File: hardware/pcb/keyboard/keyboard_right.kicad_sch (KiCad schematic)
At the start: 29 parts, among them J1 SM04B-SRSS-TB, J2 PJ320D, J3 HRO_TYPE-C-31-M-12, J4 FFC Connector, SW29 PTS845, U3 DT1446-04S, U4 XC6220B331MR-G, U5 STM32G431KBTx, Y1 8MHz

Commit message: usb hib init
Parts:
- added R9: 1k, PCM_Resistor_SMD_AKL:R_0603_1608Metric, symbol Device:R
- added R9: 10k, PCM_Resistor_SMD_AKL:R_0603_1608Metric, symbol Device:R
- added R9: 5.1k, PCM_Resistor_SMD_AKL:R_0603_1608Metric, symbol Device:R
- J4: value FFC Connector -> HRS_FH34SRJ-12S-0.5SH(50)
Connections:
- net +3V3: now also R9.2
- net ACCS_1: now also U5.9 (PA4), R9.1; no longer U5.5 (PA0)
- net ACCS_3: now also R9.1, R9.2
- net CSEL0: now also U5.5 (PA0); no longer U5.9 (PA4)
- net GND: now also R9.1
- net VBUS: now also R9.2
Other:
- note added: "ACCS_3(SPI MISO) ACCS_1(SPI CS) can be used as a extra GPIO or VBUS/USB, Handness detect"
- note added: "Pin functionalities. PA4 | |SPI1_NSS |SPI3_NSS | |USART2_CK PB3 | |SPI1_SCK |SPI3_SCK | |USART2_TX PB4 | |SPI1_MISO|SPI3_MISO| |USART2_RX PB5 | |SPI1_MOSI|SPI3_MOSI| |USART2_CK PB6 | | | |USART1_TX| PB7 |I2C1_SDA | | |USART1_RX| PB8-BOOT0|I2C1_SCL | | |"

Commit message: preproduction
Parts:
- removed U3: DT1446-04S, PCM_Package_TO_SOT_SMD_AKL:SOT-363_SC-70-6_Handsoldering, symbol Power_Protection:SRV05-4
- added U3: PRTR5V0U2X, PCM_Package_TO_SOT_SMD_AKL:SOT-143, symbol Power_Protection:PRTR5V0U2X
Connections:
- net +5V: now also U3.4 (VCC)
- net D+: now also U3.2 (I/O1)
- net D-: now also U3.3 (I/O2)
- net GND: now also U3.1 (GND)
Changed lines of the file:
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@@
-    )
-  )
-  (global_label "D-" (shape input) (at 154.94 139.7 0) (fields_autoplaced)
-    (effects (font (size 1.27 1.27)) (justify left))
-    (property "Intersheetrefs" "${INTERSHEET_REFS}" (at 159.1876 139.7 0)
-      (effects (font (size 1.27 1.27)) (justify left) hide)
     )
   )
@@
     )
   )
-  (global_label "USART_TX" (shape input) (at 154.94 144.78 0) (fields_autoplaced)
+  (global_label "D-" (shape input) (at 153.67 139.7 0) (fields_autoplaced)
     (effects (font (size 1.27 1.27)) (justify left))
-    (property "Intersheetrefs" "${INTERSHEET_REFS}" (at 165.6048 144.78 0)
+    (property "Intersheetrefs" "${INTERSHEET_REFS}" (at 157.9176 139.7 0)
       (effects (font (size 1.27 1.27)) (justify left) hide)
     )
@@
     (property "Intersheetrefs" "${INTERSHEET_REFS}" (at 253.8362 24.13 0)
       (effects (font (size 1.27 1.27)) (justify left) hide)
+    )
+  )
+  (global_label "D+" (shape input) (at 128.27 139.7 180) (fields_autoplaced)
+    (effects (font (size 1.27 1.27)) (justify right))
+    (property "Intersheetrefs" "${INTERSHEET_REFS}" (at 124.0224 139.7 0)
+      (effects (font (size 1.27 1.27)) (justify right) hide)
     )
   )
@@
     )
   )
-  (global_label "USART_RX" (shape input) (at 129.54 139.7 180) (fields_autoplaced)
-    (effects (font (size 1.27 1.27)) (justify right))
-    (property "Intersheetrefs" "${INTERSHEET_REFS}" (at 118.8752 139.7 0)
-      (effects (font (size 1.27 1.27)) (justify right) hide)
-    )
-  )
   (global_label "TX2" (shape input) (at 254 55.88 0) (fields_autoplaced)
     (effects (font (size 1.27 1.27)) (justify left))
@@
     (effects (font (size 1.27 1.27)) (justify right))
     (property "Intersheetrefs" "${INTERSHEET_REFS}" (at 237.4533 53.34 0)
-      (effects (font (size 1.27 1.27)) (justify right) hide)
-    )
-  )
-  (global_label "D+" (shape input) (at 129.54 144.78 180) (fields_autoplaced)
-    (effects (font (size 1.27 1.27)) (justify right))
-    (property "Intersheetrefs" "${INTERSHEET_REFS}" (at 125.2924 144.78 0)
       (effects (font (size 1.27 1.27)) (justify right) hide)
     )
@@
     )
   )
-  (symbol (lib_id "power:GND") (at 142.24 154.94 0) (mirror y) (unit 1)
-    (in_bom yes) (on_board yes) (dnp no)
-    (property "Reference" "#PWR022" (at 142.24 161.29 0)
-      (effects (font (size 1.27 1.27)) hide)
-    )
-    (property "Value" "GND" (at 140.97 158.75 0)
-      (effects (font (size 1.27 1.27)) (justify right))
-    )
-    (property "Footprint" "" (at 142.24 154.94 0)
-      (effects (font (size 1.27 1.27)) hide)
-    )
-    (property "Datasheet" "" (at 142.24 154.94 0)
-      (effects (font (size 1.27 1.27)) hide)
-    )
-    (pin "1")
-    (instances
-      (project "keyboard_right"
-        (path "/852dabbf-de45-4470-8176-59d37a754407"
-          (reference "#PWR022") (unit 1)
-        )
-      )
-      (project "EC60-Rev_1_1"
-        (path "/e63e39d7-6ac0-4ffd-8aa3-1841a4541b55"
-          (reference "#PWR020") (unit 1)
-        )
-      )
-    )
-  )
   (symbol (lib_id "PCM_Diode_Schottky_AKL:1N5818") (at 68.58 118.11 0) (unit 1)
     (in_bom yes) (on_board yes) (dnp no)
@@
     )
   )
+  (symbol (lib_id "Power_Protection:PRTR5V0U2X") (at 140.97 139.7 0) (unit 1)
+    (in_bom yes) (on_board yes) (dnp no)
+    (property "Reference" "U3" (at 151.13 130.81 0)
+      (effects (font (size 1.27 1.27)))
+    )
+    (property "Value" "PRTR5V0U2X" (at 154.94 133.35 0)
+      (effects (font (size 1.27 1.27)))
+    )
+    (property "Footprint" "PCM_Package_TO_SOT_SMD_AKL:SOT-143" (at 142.494 139.7 0)
+      (effects (font (size 1.27 1.27)) hide)
+    )
+    (property "Datasheet" "https://assets.nexperia.com/documents/data-sheet/PRTR5V0U2X.pdf" (at 142.494 139.7 0)
+      (effects (font (size 1.27 1.27)) hide)
+    )
+    (property "LCSC" "C2827688" (at 140.97 139.7 0)
+      (effects (font (size 1.27 1.27)) hide)
+    )
+    (pin "1")
+    (pin "2")
+    (pin "3")
+    (pin "4")
+    (instances
+      (project "keyboard_right"
+        (path "/852dabbf-de45-4470-8176-59d37a754407"
+          (reference "U3") (unit 1)
+        )
+      )
+      (project "EC60-Rev_1_1"
+        (path "/e63e39d7-6ac0-4ffd-8aa3-1841a4541b55"
+          (reference "D1") (unit 1)
+        )
+      )
+    )
+  )
   (symbol (lib_id "Device:C") (at 185.42 26.67 180) (unit 1)
     (in_bom yes) (on_board yes) (dnp no)
@@
     )
   )
+  (symbol (lib_id "power:GND") (at 140.97 152.4 0) (mirror y) (unit 1)
+    (in_bom yes) (on_board yes) (dnp no)
+    (property "Reference" "#PWR022" (at 140.97 158.75 0)
+      (effects (font (size 1.27 1.27)) hide)
+    )
+    (property "Value" "GND" (at 140.97 156.21 90)
+      (effects (font (size 1.27 1.27)) (justify right))
+    )
+    (property "Footprint" "" (at 140.97 152.4 0)
+      (effects (font (size 1.27 1.27)) hide)
+    )
+    (property "Datasheet" "" (at 140.97 152.4 0)
+      (effects (font (size 1.27 1.27)) hide)
+    )
+    (pin "1")
+    (instances
+      (project "keyboard_right"
+        (path "/852dabbf-de45-4470-8176-59d37a754407"
+          (reference "#PWR022") (unit 1)
+        )
+      )
+      (project "EC60-Rev_1_1"
+        (path "/e63e39d7-6ac0-4ffd-8aa3-1841a4541b55"
+          (reference "#PWR020") (unit 1)
+        )
+      )
+    )
+  )
   (symbol (lib_id "Device:C") (at 127 49.53 90) (mirror x) (unit 1)
     (in_bom yes) (on_board yes) (dnp no)
@@
         (path "/e63e39d7-6ac0-4ffd-8aa3-1841a4541b55"
           (reference "#PWR022") (unit 1)
-        )
-      )
-    )
-  )
-  (symbol (lib_id "power:+5V") (at 142.24 129.54 0) (unit 1)
-    (in_bom yes) (on_board yes) (dnp no)
-    (property "Reference" "#PWR020" (at 142.24 133.35 0)
-      (effects (font (size 1.27 1.27)) hide)
-    )
-    (property "Value" "+5V" (at 142.24 125.73 0)
-      (effects (font (size 1.27 1.27)))
-    )
-    (property "Footprint" "" (at 142.24 129.54 0)
-      (effects (font (size 1.27 1.27)) hide)
-    )
-    (property "Datasheet" "" (at 142.24 129.54 0)
-      (effects (font (size 1.27 1.27)) hide)
-    )
-    (pin "1")
-    (instances
-      (project "keyboard_right"
-        (path "/852dabbf-de45-4470-8176-59d37a754407"
-          (reference "#PWR020") (unit 1)
-        )
-      )
-      (project "EC60"
-        (path "/e63e39d7-6ac0-4ffd-8aa3-1841a4541b55"
-          (reference "#PWR010") (unit 1)
         )
       )
@@
     )
   )
-  (symbol (lib_id "Power_Protection:SRV05-4") (at 142.24 142.24 0) (unit 1)
-    (in_bom yes) (on_board yes) (dnp no) (fields_autoplaced)
-    (property "Reference" "U3" (at 145.3897 128.27 0)
-      (effects (font (size 1.27 1.27)) (justify left))
-    )
-    (property "Value" "DT1446-04S" (at 145.3897 130.81 0)
-      (effects (font (size 1.27 1.27)) (justify left))
-    )
-    (property "Footprint" "PCM_Package_TO_SOT_SMD_AKL:SOT-363_SC-70-6_Handsoldering" (at 160.02 153.67 0)
-      (effects (font (size 1.27 1.27)) hide)
-    )
-    (property "Datasheet" "http://www.onsemi.com/pub/Collateral/SRV05-4-D.PDF" (at 142.24 142.24 0)
-      (effects (font (size 1.27 1.27)) hide)
-    )
-    (property "Comment" "" (at 142.24 142.24 0)
-      (effects (font (size 1.27 1.27)) hide)
-    )
-    (pin "1")
-    (pin "2")
-    (pin "3")
-    (pin "4")
-    (pin "5")
-    (pin "6")
-    (instances
-      (project "keyboard_right"
-        (path "/852dabbf-de45-4470-8176-59d37a754407"
-          (reference "U3") (unit 1)
-        )
-      )
+  (symbol (lib_id "power:+5V") (at 140.97 127 0) (unit 1)
+    (in_bom yes) (on_board yes) (dnp no)
+    (property "Reference" "#PWR020" (at 140.97 130.81 0)
+      (effects (font (size 1.27 1.27)) hide)
+    )
+    (property "Value" "+5V" (at 140.97 123.19 0)
+      (effects (font (size 1.27 1.27)))
+    )
+    (property "Footprint" "" (at 140.97 127 0)
+      (effects (font (size 1.27 1.27)) hide)
+    )
+    (property "Datasheet" "" (at 140.97 127 0)
+      (effects (font (size 1.27 1.27)) hide)
+    )
+    (pin "1")
+    (instances
+      (project "keyboard_right"
+        (path "/852dabbf-de45-4470-8176-59d37a754407"
+          (reference "#PWR020") (unit 1)
+        )
+      )
+      (project "EC60"
+        (path "/e63e39d7-6ac0-4ffd-8aa3-1841a4541b55"
+          (reference "#PWR010") (unit 1)
+        )
+      )

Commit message: temp
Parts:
- C1, C20, C21: footprint PCM_Capacitor_SMD_AKL:C_0603_1608Metric_Pad1.05x0.95mm -> PCM_Capacitor_SMD_AKL:C_0603_1608Metric
- C6, C7: value 22p -> 10pF
- R9: footprint PCM_Resistor_SMD_AKL:R_0603_1608Metric_Pad0.98x0.95mm -> PCM_Resistor_SMD_AKL:R_0603_1608Metric
- Y1: value 8MHz -> 8MHz 10pF

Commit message: rev2
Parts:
- added R8: 1k, PCM_Resistor_SMD_AKL:R_0603_1608Metric, symbol Device:R
- J1: footprint Connector_JST:JST_SH_SM04B-SRSS-TB_1x04-1MP_P1.00mm_Horizontal -> Connector_JST:JST_SH_SM03B-SRSS-TB_1x03-1MP_P1.00mm_Horizontal; symbol Connector_Generic_MountingPin:Conn_01x04_MountingPin -> Connector_Generic_MountingPin:Conn_01x03_MountingPin
- renumbered C21 to C8, C20 to C9, R9 to R1, R9 to R2, R9 to R3, R9 to R4, R9 to R5
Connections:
- net +3V3: no longer J1.1 (Pin_1), J4.9 (Pin_9), R9.2
- net +5V: now also J4.10 (Pin_10), J4.11 (Pin_11)
- net ACCS_1: now also R8.2; no longer R9.1
- net ACCS_3: no longer R4.1, R5.2
- net ACCS_4: now also R8.1
- net ACCS_6: now also R9.2
- net ACCS_7: now also R9.1
- net GND: now also J1.2 (Pin_2), J4.4 (Pin_4), TP1.3 (Pin_3); no longer J1.4 (Pin_4), J1.MP (MountPin), TP1.4 (Pin_4)
- net SWCLK: now also J1.1 (Pin_1), TP1.2 (Pin_2); no longer J1.3 (Pin_3), TP1.3 (Pin_3)
- net SWDIO: now also J1.3 (Pin_3), TP1.4 (Pin_4); no longer J1.2 (Pin_2), TP1.2 (Pin_2)
- net VBUS: no longer J4.12 (Pin_12)
- net ACCS_5 renamed PB6
- net PB6: now also R4.1, R5.2; no longer J4.4 (Pin_4)
- no-connect marks 11 -> 12
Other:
- note removed: "ACCS_3(SPI MISO) ACCS_1(SPI CS) can be used as a extra GPIO or VBUS/USB, Handness detect"
- moved on the sheet: R4, R5

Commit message: init memory
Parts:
- removed R9: 1k, PCM_Resistor_SMD_AKL:R_0603_1608Metric, symbol Device:R
- added C14: 10n, PCM_Capacitor_SMD_AKL:C_0603_1608Metric, symbol Device:C
- added U6: 24FC01T-I/OT, SOT-23-5_2P9X1P6_MCH, symbol 24FC01T-I/OT:24FC01T-I_OT
- J4: value HRS_FH34SRJ-12S-0.5SH(50) -> HRS_FH34SRJ-06S-0.5SH(50); footprint ec_parts:HRS_FH34SRJ-12S-0.5SH(50) -> ec_parts:CONN6x1_FH34SRJ-6S-0.5SH50_HIR; symbol Connector_Generic_MountingPin:Conn_01x12_MountingPin -> Connector_Generic_MountingPin:Conn_01x06_MountingPin
- SW29: symbol Switch:SW_Push -> ec_parts:SW_Push
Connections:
- net +3V3: now also J4.6 (Pin_6), C14.1
- net +5V: no longer J4.10 (Pin_10), J4.11 (Pin_11)
- net ACCS_1: now also J4.5 (Pin_5); no longer J4.8 (Pin_8)
- net ACCS_2: now also J4.4 (Pin_4); no longer J4.7 (Pin_7)
- net ACCS_3: now also J4.3 (Pin_3); no longer J4.6 (Pin_6)
- net ACCS_4: now also J4.2 (Pin_2); no longer J4.5 (Pin_5)
- net GND: now also U6.2 (VSS), U6.5 (WP); no longer C13.2, J4.4 (Pin_4), J4.MP (MountPin)
- net VDDA: no longer C13.1
- net ACCS_6 renamed I2C1_SDA
- net I2C1_SDA: now also U6.3 (SDA); no longer J4.3 (Pin_3)
- net ACCS_7 renamed I2C1_SCL
- net I2C1_SCL: now also U6.1 (SCL); no longer J4.2 (Pin_2)
- new net: C14.2, U6.4 (VCC)
- no-connect marks 12 -> 10
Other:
- moved on the sheet: C13

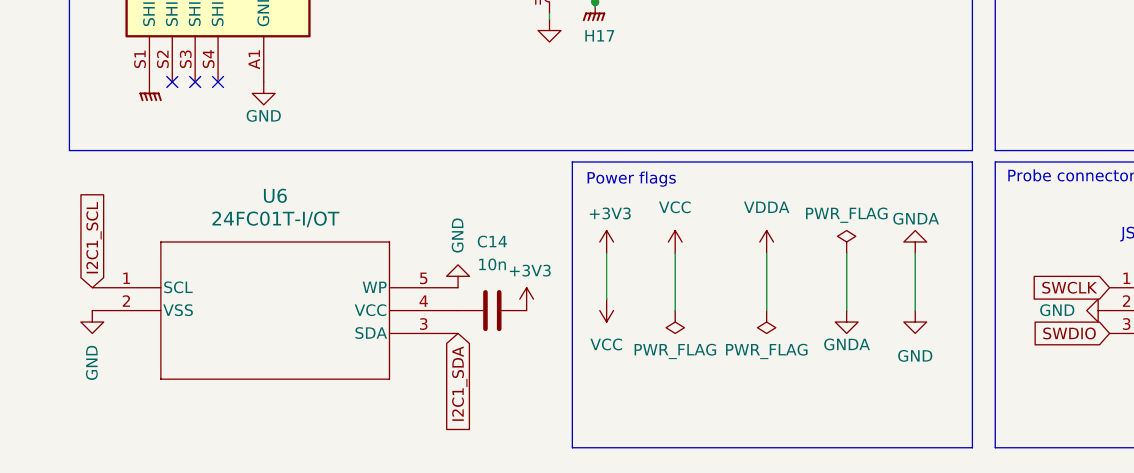
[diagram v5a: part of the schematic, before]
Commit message: add pull up register for I2C.
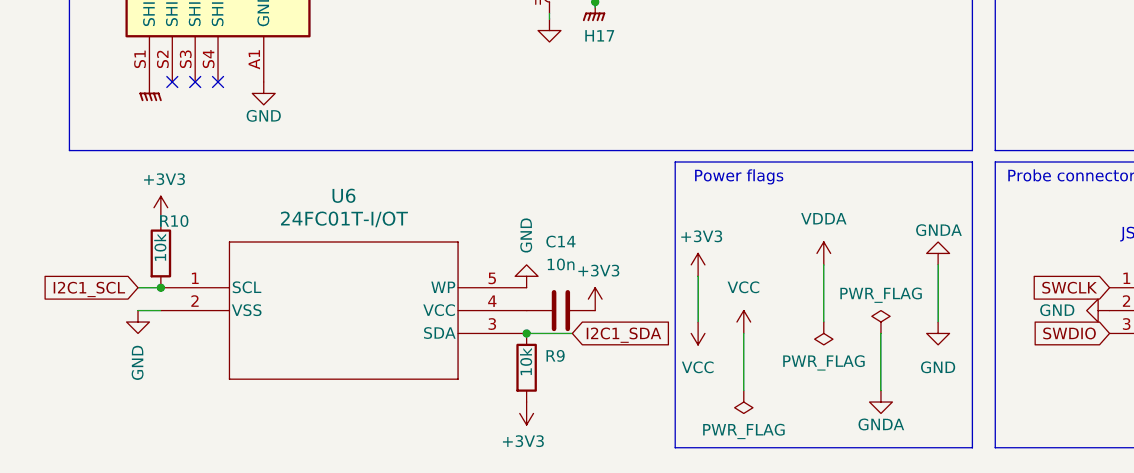
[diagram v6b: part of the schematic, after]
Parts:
- added R10, R9: 10k, PCM_Resistor_SMD_AKL:R_0603_1608Metric, symbol Device:R
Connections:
- net +3V3: now also R10.1, R9.2
- net I2C1_SCL: now also R10.2
- net I2C1_SDA: now also R9.1
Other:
- moved on the sheet: C14, U6

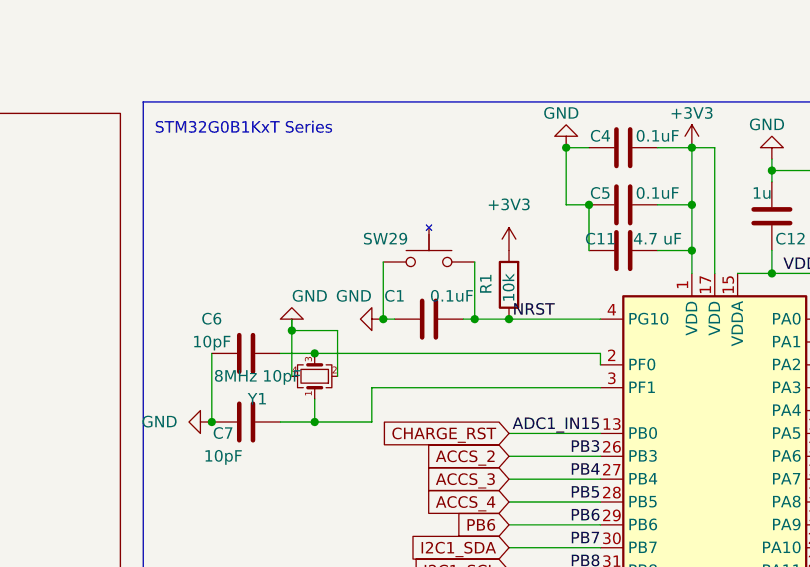
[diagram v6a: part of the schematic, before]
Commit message: fix acc connection.
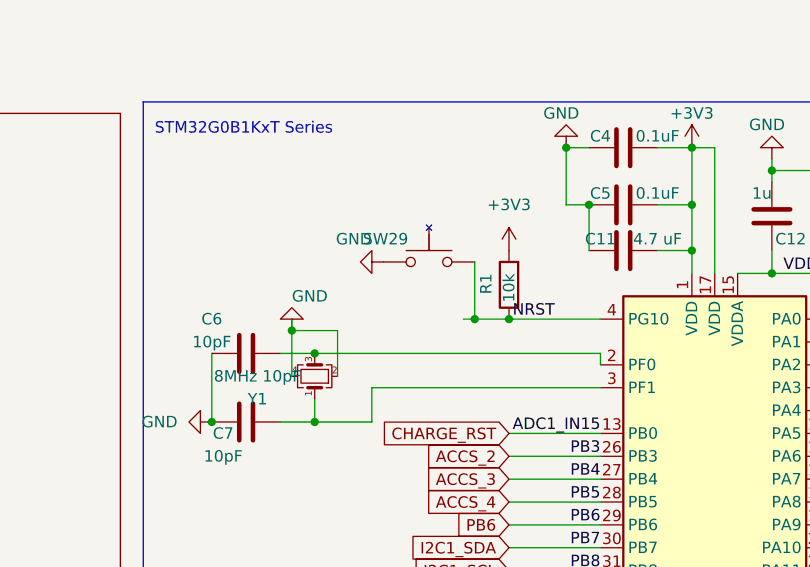
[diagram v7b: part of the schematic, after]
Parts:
- removed C1: 0.1uF, PCM_Capacitor_SMD_AKL:C_0603_1608Metric, symbol Device:C
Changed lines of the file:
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@@
 	)
 	(junction
-		(at 142.24 38.1)
-		(diameter 0)
-		(color 0 0 0 0)
-	)
-	(junction
 		(at 52.07 123.19)
 		(diameter 0)
@@
 	(wire
 		(pts
-			(xy 142.24 38.1) (xy 142.24 31.75)
-		)
-		(stroke
-			(width 0)
-			(type default)
-		)
-	)
-	(wire
-		(pts
 			(xy 156.21 60.96) (xy 166.37 60.96)
 		)
@@
 	(wire
 		(pts
-			(xy 143.51 38.1) (xy 142.24 38.1)
-		)
-		(stroke
-			(width 0)
-			(type default)
-		)
-	)
-	(wire
-		(pts
 			(xy 152.4 31.75) (xy 152.4 38.1)
 		)
@@
 	)
 	(symbol
-		(lib_id "Device:C")
-		(at 147.32 38.1 90)
-		(mirror x)
-		(unit 1)
-		(exclude_from_sim no)
-		(in_bom yes)
-		(on_board yes)
-		(dnp no)
-		(property "Reference" "C1"
-			(at 143.51 35.56 90)
-			(effects
-				(font
-					(size 1.27 1.27)
-				)
-			)
-		)
-		(property "Value" "0.1uF"
-			(at 149.86 35.56 90)
-			(effects
-				(font
-					(size 1.27 1.27)
-				)
-			)
-		)
-		(property "Footprint" "PCM_Capacitor_SMD_AKL:C_0603_1608Metric"
-			(at 151.13 39.0652 0)
-			(effects
-				(font
-					(size 1.27 1.27)
-				)
-				(hide yes)
-			)
-		)
-		(property "Datasheet" "~"
-			(at 147.32 38.1 0)
-			(effects
-				(font
-					(size 1.27 1.27)
-				)
-				(hide yes)
-			)
-		)
-		(property "Description" ""
-			(at 147.32 38.1 0)
-			(effects
-				(font
-					(size 1.27 1.27)
-				)
-				(hide yes)
-			)
-		)
-		(property "LCSC" "C307331"
-			(at 147.32 38.1 0)
-			(effects
-				(font
-					(size 1.27 1.27)
-				)
-				(hide yes)
-			)
-		)
-		(pin "1"
-		)
-		(pin "2"
-		)
-		(instances
-			(project "keyboard_right"
-				(path "/852dabbf-de45-4470-8176-59d37a754407"
-					(reference "C1")
-					(unit 1)
-				)
-			)
-			(project "EC60-Rev_1_1"
-				(path "/e63e39d7-6ac0-4ffd-8aa3-1841a4541b55"
-					(reference "C5")
-					(unit 1)
-				)
-			)
-		)
-	)
-	(symbol
 		(lib_id "Connector_Audio:AudioJack4")
 		(at 149.86 105.41 0)
@@
 		(dnp no)
 		(fields_autoplaced yes)
-		(property "Reference" "#PWR08"
+		(property "Reference" "#PWR0102"
 			(at 87.63 187.96 0)
 			(effects
@@
 			(project "keyboard_right"
 				(path "/852dabbf-de45-4470-8176-59d37a754407"
-					(reference "#PWR08")
+					(reference "#PWR0102")
 					(unit 1)
 				)
@@
 	(symbol
 		(lib_id "power:GND")
-		(at 142.24 38.1 270)
-		(unit 1)
-		(exclude_from_sim no)
-		(in_bom yes)
-		(on_board yes)
-		(dnp no)
-		(property "Reference" "#PWR011"
-			(at 135.89 38.1 0)
-			(effects
-				(font
-					(size 1.27 1.27)
-				)
-				(hide yes)
-			)
-		)
-		(property "Value" "GND"
-			(at 140.97 35.56 90)
-			(effects
-				(font
-					(size 1.27 1.27)
-				)
-				(justify right)
-			)
-		)
-		(property "Footprint" ""
-			(at 142.24 38.1 0)
-			(effects
-				(font
-					(size 1.27 1.27)
-				)
-				(hide yes)
-			)
-		)
-		(property "Datasheet" ""
-			(at 142.24 38.1 0)
-			(effects
-				(font
-					(size 1.27 1.27)
-				)
-				(hide yes)
-			)
-		)
-		(property "Description" ""
-			(at 142.24 38.1 0)
-			(effects
-				(font
-					(size 1.27 1.27)
-				)
-				(hide yes)
-			)
-		)
-		(pin "1"
-		)
-		(instances
-			(project "keyboard_right"
-				(path "/852dabbf-de45-4470-8176-59d37a754407"
-					(reference "#PWR011")
-					(unit 1)
-				)
-			)
-			(project "EC60-Rev_1_1"
-				(path "/e63e39d7-6ac0-4ffd-8aa3-1841a4541b55"
-					(reference "#PWR020")
-					(unit 1)
-				)
-			)
-		)
-	)
-	(symbol
-		(lib_id "power:GND")
 		(at 20.32 181.61 0)
 		(mirror y)
@@
 	)
 	(symbol
+		(lib_id "power:GND")
+		(at 142.24 31.75 270)
+		(unit 1)
+		(exclude_from_sim no)
+		(in_bom yes)
+		(on_board yes)
+		(dnp no)
+		(property "Reference" "#PWR011"
+			(at 135.89 31.75 0)
+			(effects
+				(font
+					(size 1.27 1.27)
+				)
+				(hide yes)
+			)
+		)
+		(property "Value" "GND"
+			(at 140.97 29.21 90)
+			(effects
+				(font
+					(size 1.27 1.27)
+				)
+				(justify right)
+			)
+		)
+		(property "Footprint" ""
+			(at 142.24 31.75 0)
+			(effects
+				(font
+					(size 1.27 1.27)
+				)
+				(hide yes)
+			)
+		)
+		(property "Datasheet" ""
+			(at 142.24 31.75 0)
+			(effects
+				(font
+					(size 1.27 1.27)
+				)
+				(hide yes)
+			)
+		)
+		(property "Description" ""
+			(at 142.24 31.75 0)
+			(effects
+				(font
+					(size 1.27 1.27)
+				)
+				(hide yes)
+			)
+		)
+		(pin "1"
+		)
+		(instances
+			(project "keyboard_right"
+				(path "/852dabbf-de45-4470-8176-59d37a754407"
+					(reference "#PWR011")
+					(unit 1)
+				)
+			)
+		)
+	)
+	(symbol
 		(lib_id "power:PWR_FLAG")
 		(at 96.52 182.88 180)
@@
 		(on_board yes)
 		(dnp no)
-		(property "Reference" "#PWR04"
+		(property "Reference" "#PWR0101"
 			(at 82.55 181.61 0)
 			(effects
@@
 			(project "keyboard_right"
 				(path "/852dabbf-de45-4470-8176-59d37a754407"
-					(reference "#PWR04")
+					(reference "#PWR0101")
 					(unit 1)
 				)

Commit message: update schema.
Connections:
- net ACCS_1 renamed PA4
- net ACCS_2 renamed PB3
- net ACCS_3 renamed PB4
- net ACCS_4 renamed PB5
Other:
- note added: "Handness"
- note added: "Pin functionalities. PA4 | |SPI1_NSS |SPI3_NSS | |USART2_CK PB3 | |SPI1_SCK |SPI3_SCK | |USART2_TX PB4 | |SPI1_MISO|SPI3_MISO| |USART2_RX PB5 | |SPI1_MOSI|SPI3_MOSI| |USART2_CK"
- note removed: "Pin functionalities. PA4 | |SPI1_NSS |SPI3_NSS | |USART2_CK PB3 | |SPI1_SCK |SPI3_SCK | |USART2_TX PB4 | |SPI1_MISO|SPI3_MISO| |USART2_RX PB5 | |SPI1_MOSI|SPI3_MOSI| |USART2_CK PB6 | | | |USART1_TX| PB7 |I2C1_SDA | | |USART1_RX| PB8-BOOT0|I2C1_SCL | | |"
- company: (none) -> https://github.com/daehyeok/Corne_EEC
- moved on the sheet: C14, R10, R8, R9, U6
